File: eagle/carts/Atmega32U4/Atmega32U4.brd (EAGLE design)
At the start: 50.2 x 61 mm, 30 parts, among them J6 USB4110-GF-A_REVB, U1 3.3V, U3 32U4, X3 16MHz

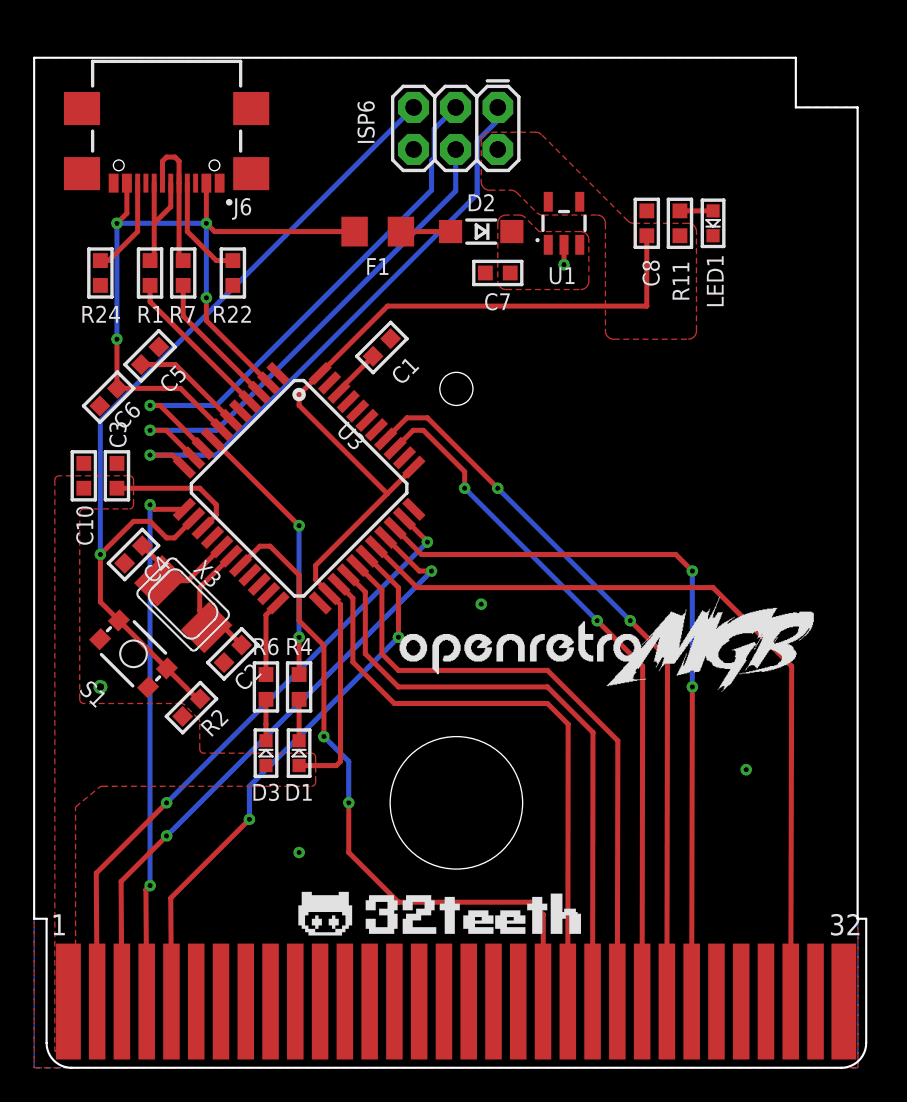
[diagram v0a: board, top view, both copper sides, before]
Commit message: feat: update USB and VCC lines on ATMega
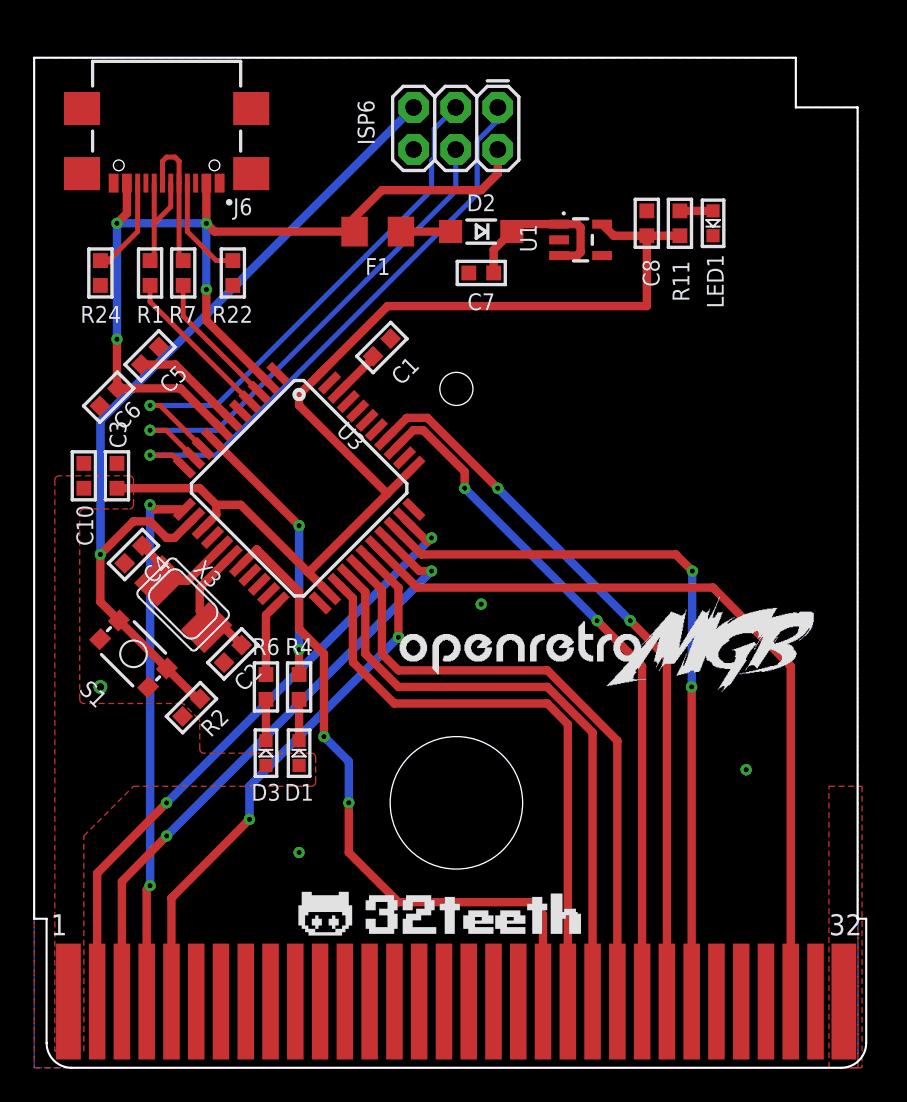
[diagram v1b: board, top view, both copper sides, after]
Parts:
- R1, R7: value 5.1K -> 22
- moved U1 1.41 mm to (33.0, 50.0), turned to 270 degrees
- moved C7 1.00 mm to (27.0, 48.0)
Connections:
- net 3V3: no longer ISP6.2
- net V_USB: now also ISP6.2
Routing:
- net V_USB: track 48.2 -> 60.4 mm
- net RAW: track 0.00 -> 10.3 mm
- net GND: track 1.20 -> 0.00 mm, vias 5 -> 4
- net A: track 41.3 -> 40.5 mm
- net CLK: track 38.0 -> 38.6 mm
- removed copper zone on layer 1, net RAW

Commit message: feat: redesign ATmega cartridge
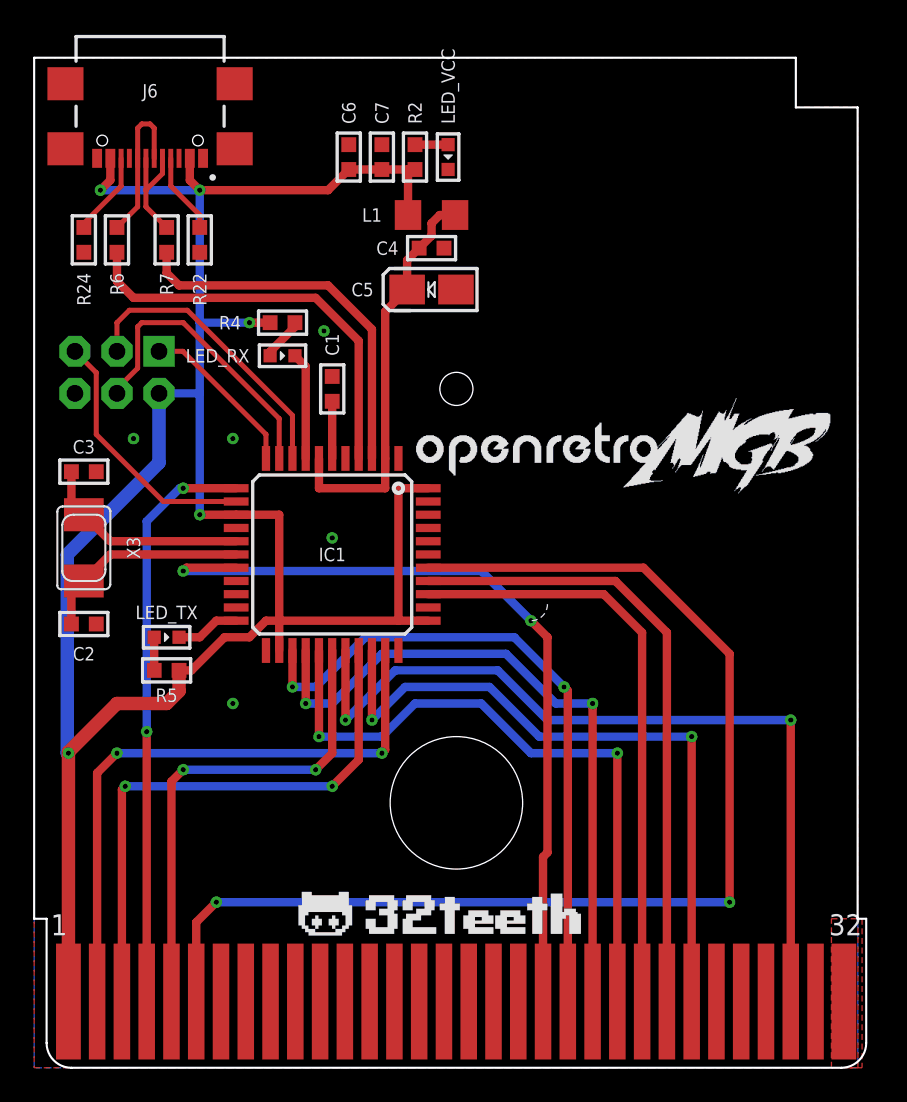
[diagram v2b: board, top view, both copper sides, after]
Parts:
- removed C10: 1.0uF, RetroESP32:0603-MINI-CAP
- removed C8: 10uF, RetroESP32:0603-MINI-CAP
- removed D1: Yellow, RetroESP32:CHIPLED_0603
- removed D2: 3A/10V/280mV, RetroESP32:SOD-123
- removed D3: GREEN, RetroESP32:CHIPLED_0603
- removed F1: 6V/0.5A, SparkFun-Fuses:1206
- removed LED1: RED, RetroESP32:CHIPLED_0603
- removed R1: 22, RetroESP32:0603-MINI
- removed R11: 1k, RetroESP32:0603-MINI
- removed S1: Reset, SparkFun-Switches:TACTILE_SWITCH_SMD_4.6X2.8MM
- removed U1: 3.3V, SparkFun-IC-Power:SOT23-5
- removed U3: 32U4, SparkFun-IC-Microcontroller:TQFP44
- added IC1: ATMEGA32U4-AU, adaprog:TQFP44
- added L1: 500mA, adafruit:R1206
- added LED_RX, LED_TX, LED_VCC: LED, RetroESP32:CHIPLED_0603
- added R5: 1K, RetroESP32:0603-MINI
- C2: value 22pF -> 18pF
- C3: value 0.1uF -> 18pF
- C4: value 22pF -> 0.1uF
- C5: value 1.0uF -> 10uF; device RetroESP32:0603-MINI-CAP -> RetroESP32:EIA3216-18/A-W
- C6: value 1.0uF -> 0.1uF
- C7: value 10uF -> 0.1uF
- ISP6: value AVR_SPI_PRG_6PTH -> AVR_SPI_PRG_6NS; device SparkFun-Connectors:2X3 -> SparkFun:2X3-NS
- R2: value 10k -> 1K
- R4: value 1k -> 1K
- R6: value 1k -> 22
- moved R2 35.9 mm to (23.0, 55.0), turned to 270 degrees
- moved R6 28.5 mm to (5.00, 50.0), turned to 90 degrees
- moved ISP6 28.0 mm to (5.00, 42.0)
- moved C4 25.8 mm to (24.0, 49.5), turned to 0 degrees
- moved R4 22.0 mm to (15.0, 45.0), turned to 180 degrees
- moved C6 20.5 mm to (19.0, 55.0), turned to 90 degrees
- moved C5 17.5 mm to (24.0, 47.0), turned to 180 degrees
- moved U$1 12.0 mm to (23.0, 35.0)
- moved C7 9.22 mm to (21.0, 55.0), turned to 90 degrees
- moved C2 9.18 mm to (3.00, 26.8), turned to 0 degrees
- moved X3 6.90 mm to (3.00, 31.4), turned to 90 degrees
- moved C1 3.91 mm to (18.0, 41.0), turned to 90 degrees
- moved R22 2.83 mm to (10.0, 50.0)
- moved R24 2.24 mm to (3.00, 50.0)
- moved R7 2.24 mm to (8.00, 50.0)
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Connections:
- removed net 3V3: C10.2, C3.2, C8.2, D1.A, D3.A, R11.2, R2.2, U$2.1, U1.5, U3.14, U3.24, U3.34, U3.44
- removed net A2: U3.38
- removed net AREF: C1.2, U3.42
- removed net AVR_RST: ISP6.5, R2.1, S1.3, S1.4, U3.13
- removed net D2/SDA: U3.19
- removed net N$1: C2.1, U3.17, X3.P$2
- removed net N$38: LED1.A, R11.1
- removed net N$5: D1.C, R4.2
- removed net RAW: C7.2, D2.C, U1.1, U1.3
- removed net UCAP: C5.2, U3.6
- removed net USB_RAW: D2.A, F1.2
- removed net V_USB: C6.2, F1.1, ISP6.2, J6.A4/B9, J6.B4/A9, U3.2, U3.7
- new net +5V: C4.1, C5.+, IC1.2, IC1.7, L1.2
- new net BATTERY-MONITOR: IC1.38, U$2.6
- new net D2: IC1.19
- new net HWB: IC1.33
- new net N$4: C1.1, IC1.6
- new net N$6: LED_RX.A, R4.1
- new net N$8: C2.1, IC1.17, X3.P$2
- new net N$9: C3.1, IC1.16, X3.P$1
- new net RST: IC1.13, ISP6.5
- new net VCC: C6.1, C7.1, IC1.14, IC1.24, IC1.34, IC1.44, ISP6.2, J6.A4/B9, J6.B4/A9, L1.1, R2.2, R4.2, R5.2, U$2.1
- net A: now also IC1.18; no longer U3.18
- net A3: now also IC1.39; no longer U3.39
- net A4: now also IC1.40; no longer U3.40
- net A5: now also IC1.41; no longer U3.41
- net AUDIO: now also IC1.31; no longer U3.31
- net AVR_MISO: now also IC1.11; no longer U3.11
- net AVR_MOSI: now also IC1.10; no longer U3.10
- net AVR_SCK: now also IC1.9; no longer U3.9
- net B: now also IC1.25; no longer U3.25
- net CLK: now also IC1.32; no longer U3.32
- net CS: now also IC1.28; no longer U3.28
- net D+: now also IC1.4, R6.1; no longer R1.1, U3.4
- net D-: now also IC1.3; no longer U3.3
- net D7: now also IC1.1; no longer U3.1
- net DC: now also IC1.30; no longer U3.30
- net DP: now also R6.2; no longer R1.2
- net DPAD-LR: now also IC1.36; no longer U3.36
- net DPAD-UD: now also IC1.37; no longer U3.37
- net GND: now also C1.2, C3.2, C5.-, C6.2, C7.2, IC1.15, IC1.23, IC1.35, IC1.43, IC1.5, LED_VCC.C; no longer C1.1, C10.1, C3.1, C5.1, C6.1, C7.1, C8.1, LED1.C, S1.1, S1.2, U1.2, U3.15, U3.23, U3.33, U3.35, U3.43, U3.5
- net MOSI: now also IC1.12; no longer U3.12
- net N$2: now also LED_VCC.A, R2.1; no longer C4.1, U3.16, X3.P$1
- net N$7: now also LED_TX.A, R5.1; no longer D3.C, R6.2
- net RESET: now also IC1.29; no longer U3.29
- net RXI: now also IC1.20; no longer U3.20
- net RXLED: now also IC1.8, LED_RX.C; no longer R4.1, U3.8
- net SELECT: now also IC1.27; no longer U3.27
- net START: now also IC1.26; no longer U3.26
- net TXLED: now also IC1.22, LED_TX.C; no longer R6.1, U3.22
- net TXO: now also IC1.21; no longer U3.21
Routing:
- net VCC: track 0.00 -> 141.1 mm, vias 0 -> 5
- net BATTERY-MONITOR: track 0.00 -> 72.9 mm, vias 0 -> 2
- net 3V3: track 66.9 -> 0.00 mm
- net V_USB: track 60.4 -> 0.00 mm, vias 4 -> 0
- net AVR_RST: track 53.5 -> 0.00 mm, vias 1 -> 0
- net +5V: track 0.00 -> 24.6 mm
- net AVR_MISO: track 34.4 -> 9.99 mm, vias 1 -> 0
- net RST: track 0.00 -> 15.7 mm
- net D+: track 9.52 -> 24.9 mm
- net D-: track 8.36 -> 22.9 mm
- net AVR_SCK: track 32.3 -> 17.9 mm, vias 1 -> 0
- net N$9: track 0.00 -> 12.8 mm
- net N$8: track 0.00 -> 12.8 mm
- net AVR_MOSI: track 30.3 -> 18.0 mm, vias 1 -> 0
- net RAW: track 10.3 -> 0.00 mm
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- removed copper zone on layer 1, net 3V3
